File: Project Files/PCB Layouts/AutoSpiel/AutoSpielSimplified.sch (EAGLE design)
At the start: 30 parts, among them X1 5566-24

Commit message: Updated the simplified schematic
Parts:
- added DA#3, DA#4, DA3, DA4, DB3, DB4, DC#3, DC#4, DC3, DC4, DC5, DD#3, DD#4, DD3, DD4, DE3, DE4, DF#3, DF#4, DF3, DF4, DG#3, DG#4, DG3, DG4: 1A/50V/1.1V, SparkFun-DiscreteSemi:DIODE-PTH
- added QA#3, QA#4, QA3, QA4, QB3, QB4, QC#3, QC#4, QC3, QC4, QC5, QD#3, QD#4, QD3, QD4, QE3, QE4, QF#3, QF#4, QF3, QF4, QG#3, QG#4, QG3, QG4: TIP120, transistor-power:TIP120
- added RA#3, RA#4, RA3, RA4, RB3, RB4, RC#3, RC#4, RC3, RC4, RC5, RD#3, RD#4, RD3, RD4, RE3, RE4, RF#3, RF#4, RF3, RF4, RG#3, RG#4, RG3, RG4: 1k, SparkFun-Resistors:1KOHM-HORIZ-1/4W-5%
- added SOLA#3, SOLA#4, SOLA3, SOLA4, SOLB3, SOLB4, SOLC#3, SOLC#4, SOLC3, SOLC4, SOLC5, SOLD#3, SOLD#4, SOLD3, SOLD4, SOLE3, SOLE4, SOLF#3, SOLF#4, SOLF3, SOLF4, SOLG#3, SOLG#4, SOLG3, SOLG4: (no value), SparkFun-Connectors:CONN_02PTH4
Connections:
- new net N$12: DD3.A, QD3.C, SOLD3.2
- new net N$15: QD#3.B, RD#3.2
- new net N$18: DD#3.A, QD#3.C, SOLD#3.2
- new net N$2: QC#3.B, RC#3.2
- new net N$21: QE3.B, RE3.2
- new net N$22: QC3.B, RC3.2
- new net N$23: DC3.A, QC3.C, SOLC3.2
- new net N$24: DE3.A, QE3.C, SOLE3.2
- new net N$25: QA3.B, RA3.2
- new net N$26: DA3.A, QA3.C, SOLA3.2
- new net N$27: QF3.B, RF3.2
- new net N$28: DF3.A, QF3.C, SOLF3.2
- new net N$29: QF#3.B, RF#3.2
- new net N$30: DF#3.A, QF#3.C, SOLF#3.2
- new net N$31: QG3.B, RG3.2
- new net N$32: DG3.A, QG3.C, SOLG3.2
- new net N$33: QG#3.B, RG#3.2
- new net N$34: DG#3.A, QG#3.C, SOLG#3.2
- new net N$35: QF4.B, RF4.2
- new net N$36: DF4.A, QF4.C, SOLF4.2
- new net N$37: QF#4.B, RF#4.2
- new net N$38: DF#4.A, QF#4.C, SOLF#4.2
- new net N$39: QG4.B, RG4.2
- new net N$40: DG4.A, QG4.C, SOLG4.2
- new net N$41: QG#4.B, RG#4.2
- new net N$42: DG#4.A, QG#4.C, SOLG#4.2
- new net N$43: QA4.B, RA4.2
- new net N$44: DA4.A, QA4.C, SOLA4.2
- new net N$45: QA#4.B, RA#4.2
- new net N$46: DA#4.A, QA#4.C, SOLA#4.2
- new net N$47: QB4.B, RB4.2
- new net N$48: DB4.A, QB4.C, SOLB4.2
- new net N$49: QC5.B, RC5.2
- new net N$50: DC5.A, QC5.C, SOLC5.2
- new net N$52: QA#3.B, RA#3.2
- new net N$53: DA#3.A, QA#3.C, SOLA#3.2
- new net N$55: QB3.B, RB3.2
- new net N$56: DB3.A, QB3.C, SOLB3.2
- new net N$58: QC4.B, RC4.2
- new net N$59: DC4.A, QC4.C, SOLC4.2
- new net N$6: DC#3.A, QC#3.C, SOLC#3.2
- new net N$61: QC#4.B, RC#4.2
- new net N$62: DC#4.A, QC#4.C, SOLC#4.2
- new net N$64: QD4.B, RD4.2
- new net N$65: DD4.A, QD4.C, SOLD4.2
- new net N$67: QD#4.B, RD#4.2
- new net N$68: DD#4.A, QD#4.C, SOLD#4.2
- new net N$70: QE4.B, RE4.2
- new net N$71: DE4.A, QE4.C, SOLE4.2
- new net N$9: QD3.B, RD3.2
- net A#3: now also RA#3.1
- net A#4: now also RA#4.1
- net A3: now also RA3.1
- net A4: now also RA4.1
- net B3: now also RB3.1
- net B4: now also RB4.1
- net C#3: now also RC#3.1
- net C#4: now also RC#4.1
- net C3: now also RC3.1
- net C4: now also RC4.1
- net C5: now also RC5.1
- net D#3: now also RD#3.1
- net D#4: now also RD#4.1
- net D3: now also RD3.1
- net D4: now also RD4.1
- net E3: now also RE3.1
- net E4: now also RE4.1
- net F#3: now also RF#3.1
- net F#4: now also RF#4.1
- net F3: now also RF3.1
- net F4: now also RF4.1
- net G#3: now also RG#3.1
- net G#4: now also RG#4.1
- net G3: now also RG3.1
- net G4: now also RG4.1
- net GND: now also QA#3.E, QA#4.E, QA3.E, QA4.E, QB3.E, QB4.E, QC#3.E, QC#4.E, QC3.E, QC4.E, QC5.E, QD#3.E, QD#4.E, QD3.E, QD4.E, QE3.E, QE4.E, QF#3.E, QF#4.E, QF3.E, QF4.E, QG#3.E, QG#4.E, QG3.E, QG4.E
- net VDD1: now also DC#3.C, DC3.C, DD#3.C, DD3.C, DE3.C, DF#3.C, DF3.C, DG#3.C, DG3.C, SOLC#3.1, SOLC3.1, SOLD#3.1, SOLD3.1, SOLE3.1, SOLF#3.1, SOLF3.1, SOLG#3.1, SOLG3.1
- net VDD2: now also DA#3.C, DA#4.C, DA3.C, DA4.C, DB3.C, DB4.C, DC#4.C, DC4.C, DC5.C, DD#4.C, DD4.C, DE4.C, DF#4.C, DF4.C, DG#4.C, DG4.C, SOLA#3.1, SOLA#4.1, SOLA3.1, SOLA4.1, SOLB3.1, SOLB4.1, SOLC#4.1, SOLC4.1, SOLC5.1, SOLD#4.1, SOLD4.1, SOLE4.1, SOLF#4.1, SOLF4.1, SOLG#4.1, SOLG4.1
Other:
- moved on the sheet: DA#2, DA2, DB2, DF#2, DF2, DG#2, DG2, QA#2, QA2, QB2, QF#2, QF2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

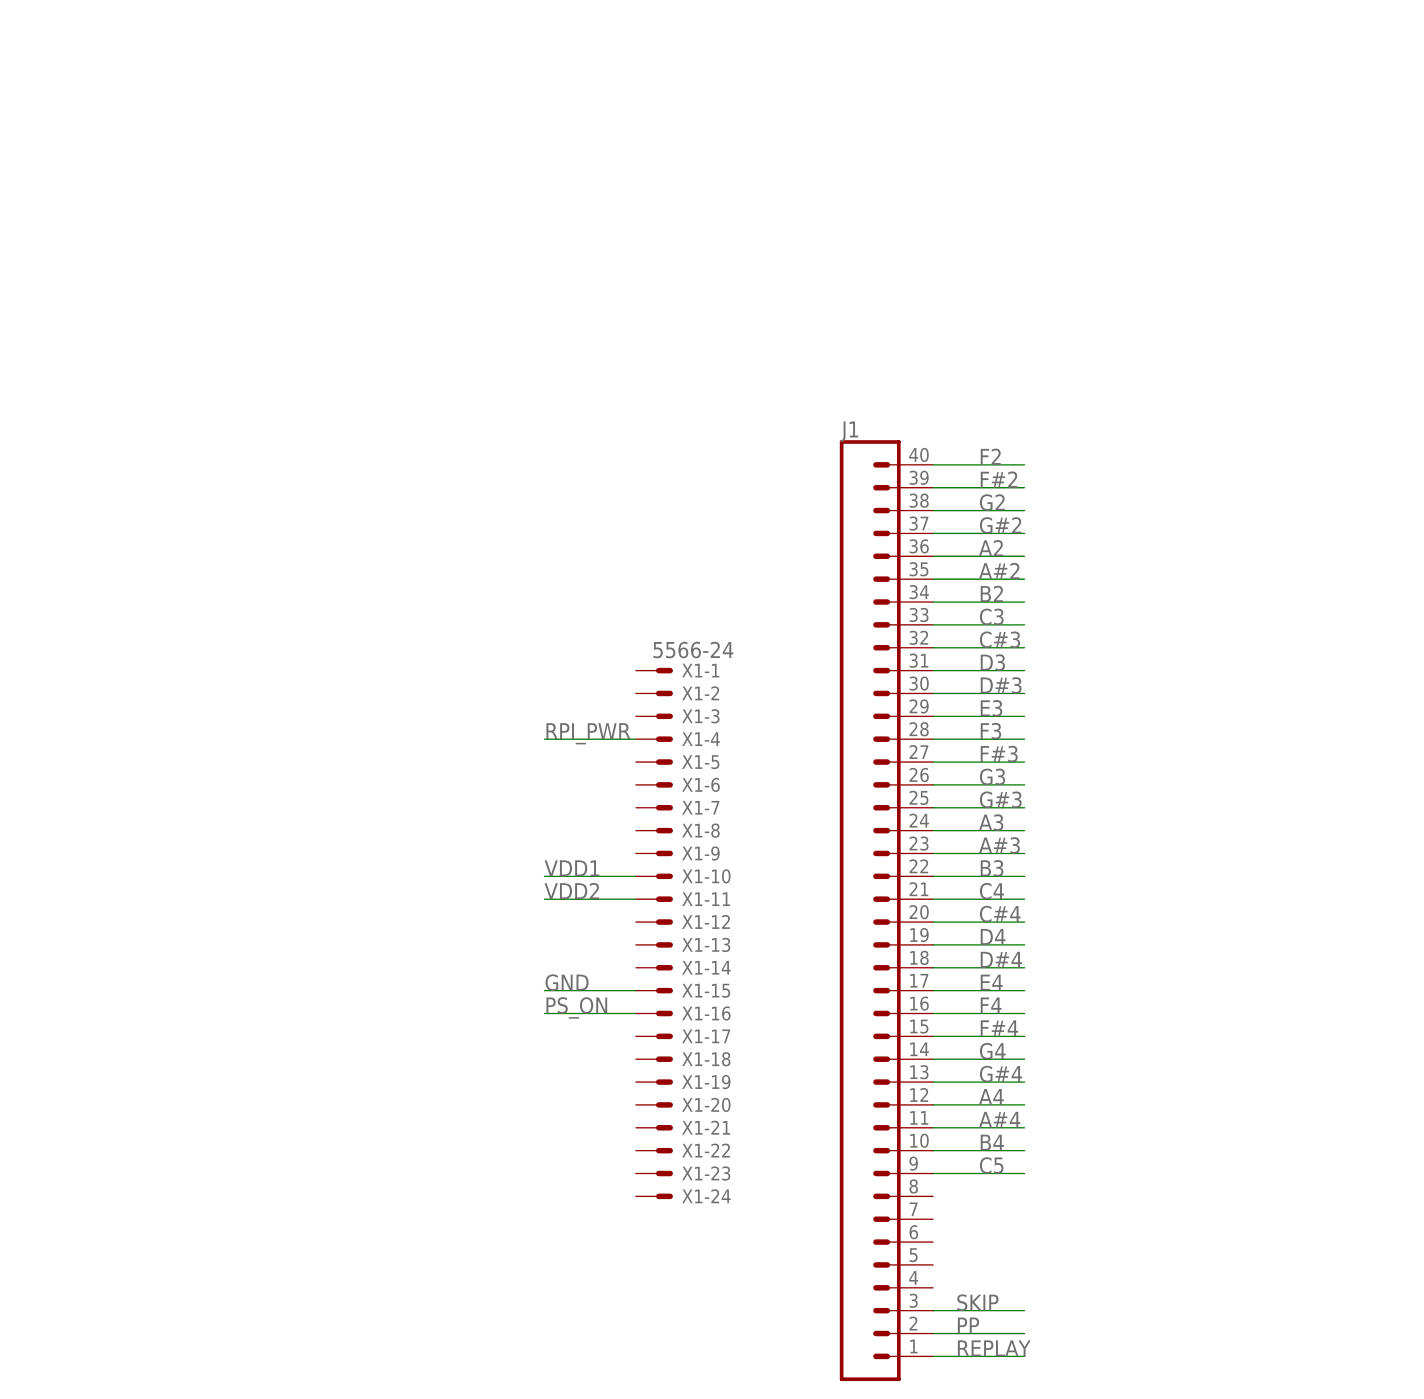
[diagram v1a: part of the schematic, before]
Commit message: Added updated schematic for the autospiel
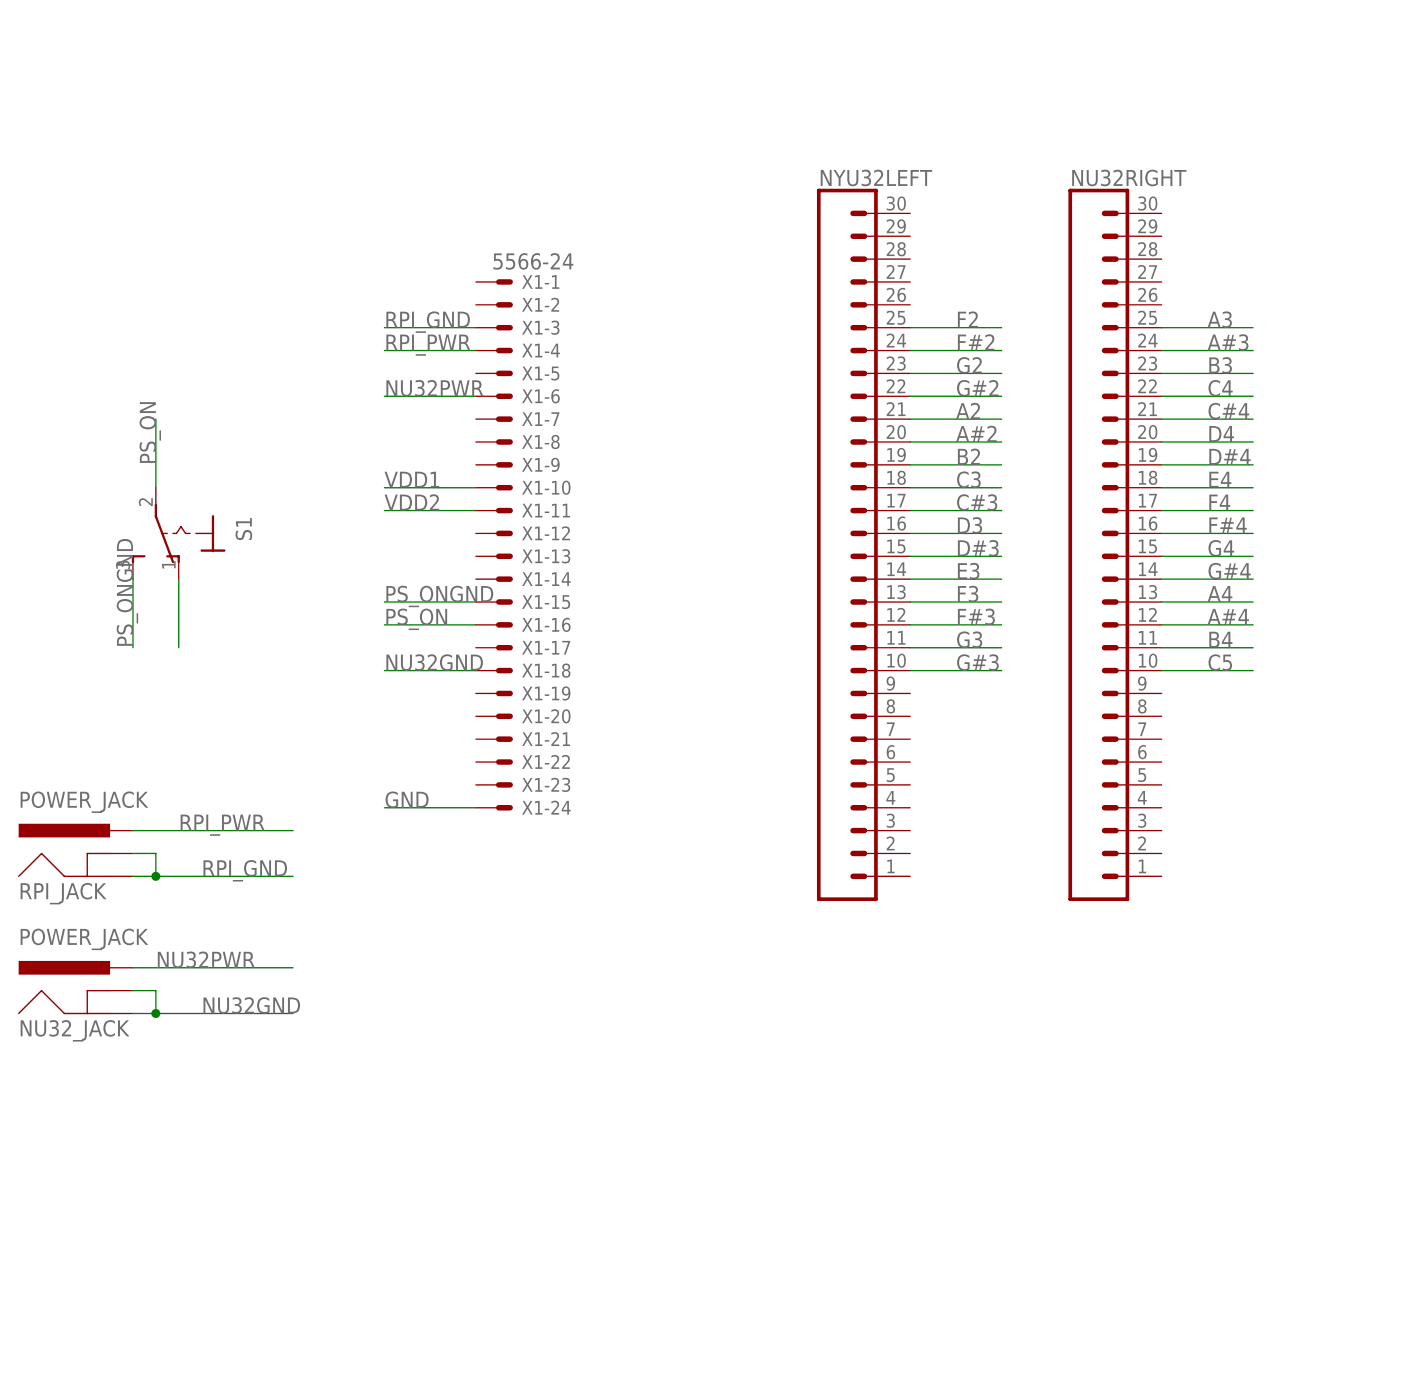
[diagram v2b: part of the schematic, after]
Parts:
- removed J1: (no value), SparkFun-Connectors:CONN_40
- added NU32RIGHT, NYU32LEFT: (no value), SparkFun-Connectors:CONN_30
- added NU32_JACK, RPI_JACK: POWER_JACK, SparkFun-Connectors:POWER_JACK
- added S1: (no value), switch:M9040P
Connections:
- removed net PP: J1.2
- removed net REPLAY: J1.1
- removed net SKIP: J1.3
- new net N$57: S1.O
- new net NU32GND: NU32_JACK.GND, NU32_JACK.GNDBREAK, X1-18.S
- new net NU32PWR: NU32_JACK.PWR, X1-6.S
- new net PS_ONGND: S1.S, X1-15.S
- new net RPI_GND: RPI_JACK.GND, RPI_JACK.GNDBREAK, X1-3.S
- net A#2: now also NYU32LEFT.20; no longer J1.35
- net A#3: now also NU32RIGHT.24; no longer J1.23
- net A#4: now also NU32RIGHT.12; no longer J1.11
- net A2: now also NYU32LEFT.21; no longer J1.36
- net A3: now also NU32RIGHT.25; no longer J1.24
- net A4: now also NU32RIGHT.13; no longer J1.12
- net B2: now also NYU32LEFT.19; no longer J1.34
- net B3: now also NU32RIGHT.23; no longer J1.22
- net B4: now also NU32RIGHT.11; no longer J1.10
- net C#3: now also NYU32LEFT.17; no longer J1.32
- net C#4: now also NU32RIGHT.21; no longer J1.20
- net C3: now also NYU32LEFT.18; no longer J1.33
- net C4: now also NU32RIGHT.22; no longer J1.21
- net C5: now also NU32RIGHT.10; no longer J1.9
- net D#3: now also NYU32LEFT.15; no longer J1.30
- net D#4: now also NU32RIGHT.19; no longer J1.18
- net D3: now also NYU32LEFT.16; no longer J1.31
- net D4: now also NU32RIGHT.20; no longer J1.19
- net E3: now also NYU32LEFT.14; no longer J1.29
- net E4: now also NU32RIGHT.18; no longer J1.17
- net F#2: now also NYU32LEFT.24; no longer J1.39
- net F#3: now also NYU32LEFT.12; no longer J1.27
- net F#4: now also NU32RIGHT.16; no longer J1.15
- net F2: now also NYU32LEFT.25; no longer J1.40
- net F3: now also NYU32LEFT.13; no longer J1.28
- net F4: now also NU32RIGHT.17; no longer J1.16
- net G#2: now also NYU32LEFT.22; no longer J1.37
- net G#3: now also NYU32LEFT.10; no longer J1.25
- net G#4: now also NU32RIGHT.14; no longer J1.13
- net G2: now also NYU32LEFT.23; no longer J1.38
- net G3: now also NYU32LEFT.11; no longer J1.26
- net G4: now also NU32RIGHT.15; no longer J1.14
- net GND: now also X1-24.S; no longer X1-15.S
- net PS_ON: now also S1.P
- net RPI_PWR: now also RPI_JACK.PWR
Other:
- moved on the sheet: X1-1, X1-10, X1-11, X1-12, X1-13, X1-14, X1-15, X1-16, X1-17, X1-18, X1-19, X1-2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
